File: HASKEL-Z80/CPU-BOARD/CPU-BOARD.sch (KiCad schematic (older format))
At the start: 85 parts, among them IC1 74LS04, IC10 Z80CPU, IC11 Z8030, IC12 Z8420, IC13 Z8420, IC14 Z8420, IC15 NE556, IC16 74HC138N, IC17 S2559E, IC18 M5205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

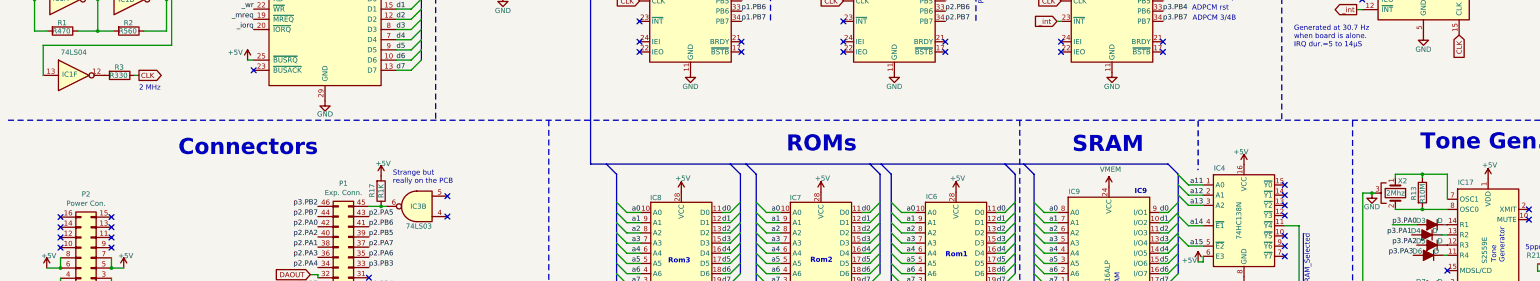
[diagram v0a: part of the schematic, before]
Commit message: Z80-ASM: PIO output example
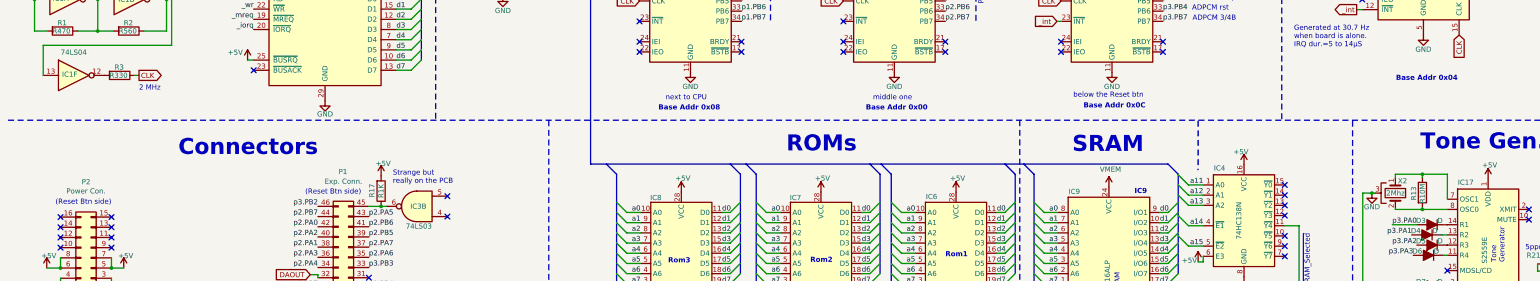
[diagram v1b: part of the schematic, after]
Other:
- note added: "(Reset Btn side)"
- note added: "Base Addr 0x00"
- note added: "Base Addr 0x04"
- note added: "Base Addr 0x08"
- note added: "Base Addr 0x0C"
- note added: "below the Reset btn"
- note added: "middle one"
- note added: "next to CPU"
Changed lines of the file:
@@
 Title "DTMF Phone central - CPU Board  - Hasler / Haskel / Ascom  "
 Date "2023-05-29"
-Rev "1.1"
+Rev "1.1b"
 Comp ""
 Comment1 "CPU Board "
@@
 U 1 1 661B042F
 P 3815 6350
-F 0 "P1" H 3865 5025 50  0000 C CNN
-F 1 "Exp. Conn." H 3865 5116 50  0000 C CNN
+F 0 "P1" H 3870 4910 50  0000 C CNN
+F 1 "Exp. Conn." H 3865 5005 50  0000 C CNN
 F 2 "" H 3815 6350 50  0001 C CNN
 F 3 "~" H 3815 6350 50  0001 C CNN
@@
 U 1 1 661BDF03
 P 1290 5755
-F 0 "P2" H 1340 5130 50  0000 C CNN
-F 1 "Power Con." H 1340 5221 50  0000 C CNN
+F 0 "P2" H 1340 5010 50  0000 C CNN
+F 1 "Power Con." H 1340 5100 50  0000 C CNN
 F 2 "" H 1290 5755 50  0001 C CNN
 F 3 "~" H 1290 5755 50  0001 C CNN
@@
 Text Notes 4210 11075 0    50   ~ 10
 Remove IC15 to disable the watchdog\n
+Text Label 7510 8460 0    50   ~ 0
+_Rom1ce
+Text Notes 8635 8885 0    50   ~ 0
+RAM_Selected
+Text Notes 13250 6005 1    50   ~ 0
+~RAM_Selected
 Wire Bus Line
 	6190 4835 11855 4835
@@
 Wire Bus Line
 	4530 1040 4530 3815
-Text Label 7510 8460 0    50   ~ 0
-_Rom1ce
-Text Notes 8635 8885 0    50   ~ 0
-RAM_Selected
-Text Notes 13250 6005 1    50   ~ 0
-~RAM_Selected
+Text Notes 3390 5140 0    50   ~ 0
+(Reset Btn side)
+Text Notes 940  5240 0    50   ~ 0
+(Reset Btn side)
+Text Notes 6925 4215 0    50   ~ 0
+next to CPU
+Text Notes 8960 4215 0    50   ~ 0
+middle one
+Text Notes 10925 4190 0    50   ~ 0
+below the Reset btn
+Text Notes 6855 4315 0    50   ~ 10
+Base Addr 0x08
+Text Notes 8890 4315 0    50   ~ 10
+Base Addr 0x00
+Text Notes 11025 4295 0    50   ~ 10
+Base Addr 0x0C
+Text Notes 14090 4025 0    50   ~ 10
+Base Addr 0x04
 $EndSCHEMATC
